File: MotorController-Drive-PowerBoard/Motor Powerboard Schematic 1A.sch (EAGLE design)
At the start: 72 parts, among them J3 APP_2POS_CONFIG5V_HORIZ, Q1 MOSFET-NCHANNELFQP30N06L, Q2 MOSFET-NCHANNELFQP30N06L, Q3 MOSFET-NCHANNELFQP30N06L, Q4 MOSFET-NCHANNELFQP30N06L, Q5 MOSFET-NCHANNELFQP30N06L, Q6 MOSFET-NCHANNELFQP30N06L, U1 NUP4201MR6

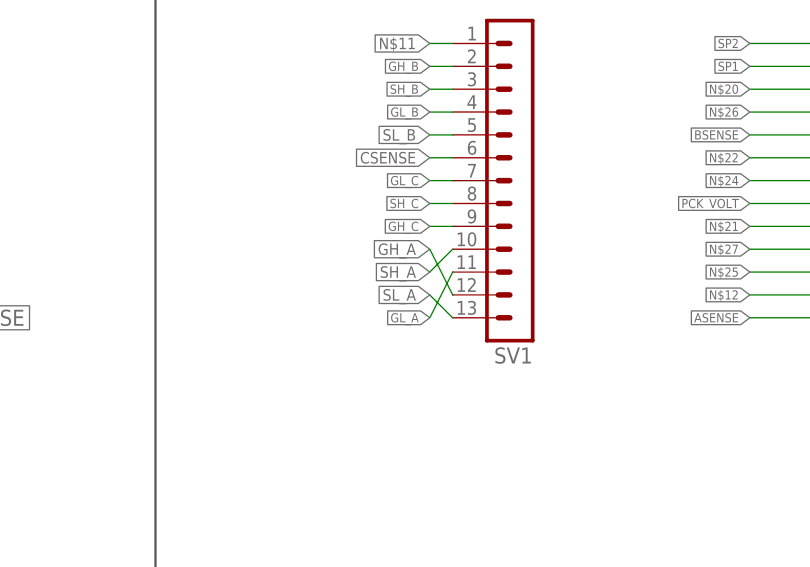
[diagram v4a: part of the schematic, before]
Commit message: Quick Routing and Labeling Fix
Straigtenned header names and made sure polygons stretched to same length on board.
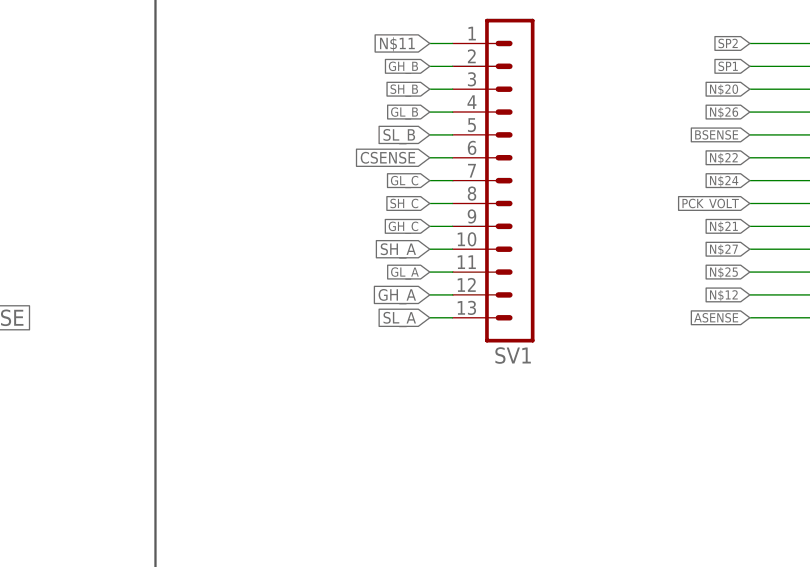
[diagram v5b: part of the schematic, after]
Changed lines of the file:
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@@
 <segment>
 <pinref part="SV1" gate="G$1" pin="13"/>
-<wire x1="172.72" y1="-43.18" x2="170.18" y2="-40.64" width="0.1524" layer="91"/>
-<label x="170.18" y="-40.64" size="1.27" layer="95" rot="R180" xref="yes"/>
+<wire x1="172.72" y1="-43.18" x2="170.18" y2="-43.18" width="0.1524" layer="91"/>
+<label x="170.18" y="-43.18" size="1.27" layer="95" rot="R180" xref="yes"/>
 </segment>
 </net>
@@
 <segment>
 <pinref part="SV1" gate="G$1" pin="11"/>
-<wire x1="172.72" y1="-38.1" x2="170.18" y2="-43.18" width="0.1524" layer="91"/>
-<label x="170.18" y="-43.18" size="1.016" layer="95" rot="R180" xref="yes"/>
+<wire x1="172.72" y1="-38.1" x2="170.18" y2="-38.1" width="0.1524" layer="91"/>
+<label x="170.18" y="-38.1" size="1.016" layer="95" rot="R180" xref="yes"/>
 </segment>
 </net>
@@
 <segment>
 <pinref part="SV1" gate="G$1" pin="12"/>
-<wire x1="172.72" y1="-40.64" x2="170.18" y2="-35.56" width="0.1524" layer="91"/>
-<label x="170.18" y="-35.56" size="1.27" layer="95" rot="R180" xref="yes"/>
+<wire x1="172.72" y1="-40.64" x2="170.18" y2="-40.64" width="0.1524" layer="91"/>
+<label x="170.18" y="-40.64" size="1.27" layer="95" rot="R180" xref="yes"/>
 </segment>
 </net>
@@
 <segment>
 <pinref part="SV1" gate="G$1" pin="10"/>
-<wire x1="172.72" y1="-35.56" x2="170.18" y2="-38.1" width="0.1524" layer="91"/>
-<label x="170.18" y="-38.1" size="1.27" layer="95" rot="R180" xref="yes"/>
+<wire x1="172.72" y1="-35.56" x2="170.18" y2="-35.56" width="0.1524" layer="91"/>
+<label x="170.18" y="-35.56" size="1.27" layer="95" rot="R180" xref="yes"/>
 </segment>
 </net>

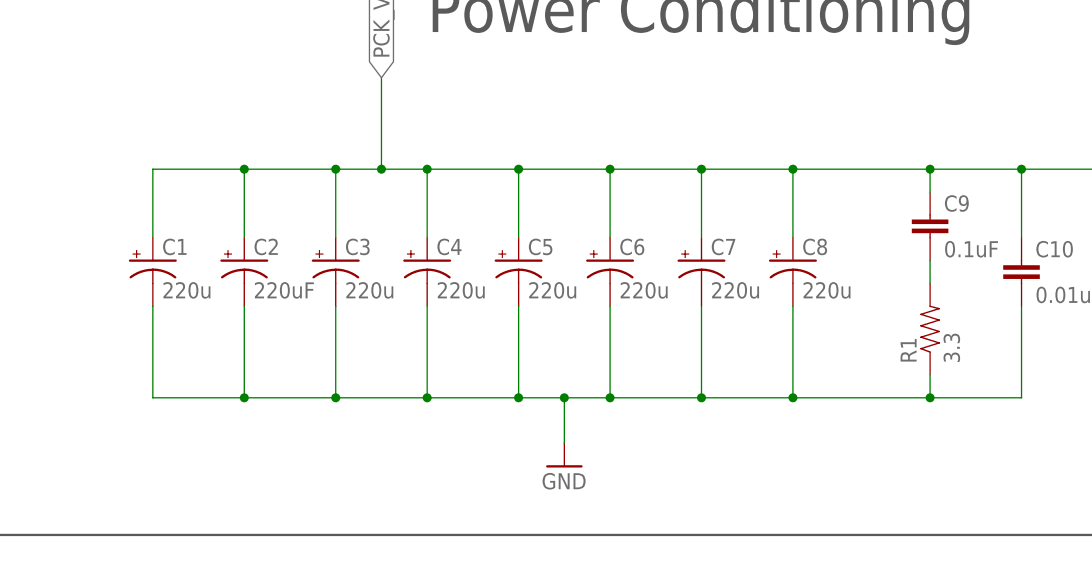
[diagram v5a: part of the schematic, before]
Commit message: Easier Viewing of Polygons. Replaced Caps
Caps now have a value of 470uF and all polygons are now easily visible so that all users can access information regarding polygons. Also all clearance issues have been resolved. Board still needs silk screen touches.
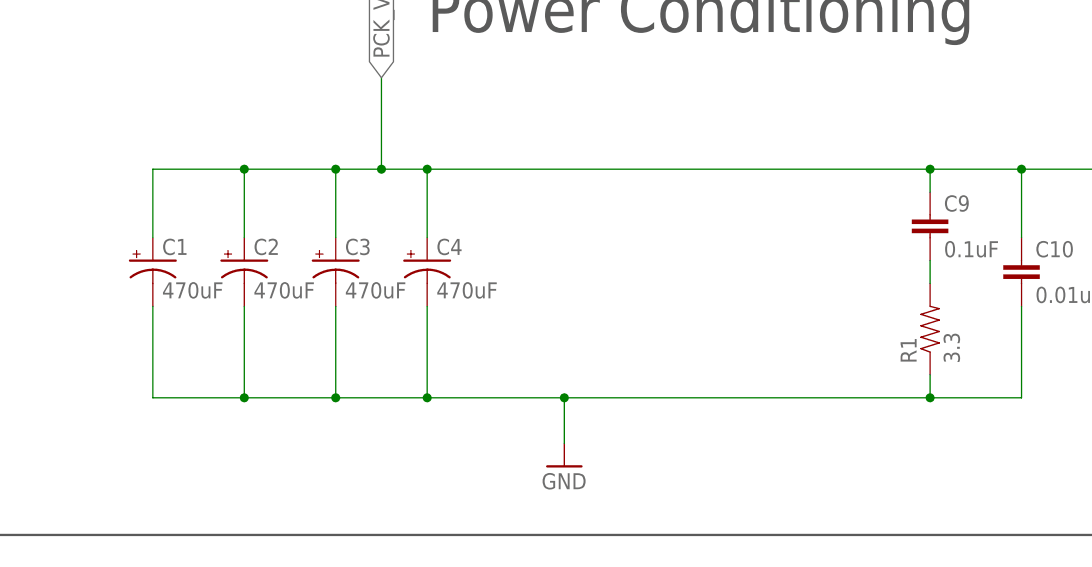
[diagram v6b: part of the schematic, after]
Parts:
- removed C5, C6, C7, C8: 220u, SparkFun-Passives:CAP_POLPTH4
- C1, C3, C4: value 220u -> 470uF
- C2: value 220uF -> 470uF
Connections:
- net GND: no longer C5.-, C6.-, C7.-, C8.-
- net PCK_VOLT: no longer C5.+, C6.+, C7.+, C8.+
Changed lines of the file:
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@@
 </classes>
 <parts>
-<part name="C1" library="SparkFun-Passives" deviceset="CAP_POL" device="PTH4" value="220u"/>
-<part name="C2" library="SparkFun-Passives" deviceset="CAP_POL" device="PTH4" value="220uF"/>
-<part name="C3" library="SparkFun-Passives" deviceset="CAP_POL" device="PTH4" value="220u"/>
-<part name="C4" library="SparkFun-Passives" deviceset="CAP_POL" device="PTH4" value="220u"/>
-<part name="C5" library="SparkFun-Passives" deviceset="CAP_POL" device="PTH4" value="220u"/>
-<part name="C6" library="SparkFun-Passives" deviceset="CAP_POL" device="PTH4" value="220u"/>
-<part name="C7" library="SparkFun-Passives" deviceset="CAP_POL" device="PTH4" value="220u"/>
-<part name="C8" library="SparkFun-Passives" deviceset="CAP_POL" device="PTH4" value="220u"/>
+<part name="C1" library="SparkFun-Passives" deviceset="CAP_POL" device="PTH4" value="470uF"/>
+<part name="C2" library="SparkFun-Passives" deviceset="CAP_POL" device="PTH4" value="470uF"/>
+<part name="C3" library="SparkFun-Passives" deviceset="CAP_POL" device="PTH4" value="470uF"/>
+<part name="C4" library="SparkFun-Passives" deviceset="CAP_POL" device="PTH4" value="470uF"/>
 <part name="R1" library="SparkFun-Passives" deviceset="RESISTOR" device="1206" value="3.3"/>
 <part name="GND1" library="SparkFun-Aesthetics" deviceset="GND" device=""/>
@@
 <instance part="C3" gate="G$1" x="-190.5" y="45.72"/>
 <instance part="C4" gate="G$1" x="-180.34" y="45.72"/>
-<instance part="C5" gate="G$1" x="-170.18" y="45.72"/>
-<instance part="C6" gate="G$1" x="-160.02" y="45.72"/>
-<instance part="C7" gate="G$1" x="-149.86" y="45.72"/>
-<instance part="C8" gate="G$1" x="-139.7" y="45.72"/>
 <instance part="R1" gate="G$1" x="-124.46" y="38.1" rot="R90"/>
 <instance part="GND1" gate="1" x="-165.1" y="22.86"/>
@@
 <wire x1="-210.82" y1="40.64" x2="-210.82" y2="30.48" width="0.1524" layer="91"/>
 <wire x1="-210.82" y1="30.48" x2="-200.66" y2="30.48" width="0.1524" layer="91"/>
-<pinref part="C8" gate="G$1" pin="-"/>
 <wire x1="-200.66" y1="30.48" x2="-190.5" y2="30.48" width="0.1524" layer="91"/>
 <wire x1="-190.5" y1="30.48" x2="-180.34" y2="30.48" width="0.1524" layer="91"/>
-<wire x1="-180.34" y1="30.48" x2="-170.18" y2="30.48" width="0.1524" layer="91"/>
-<wire x1="-170.18" y1="30.48" x2="-165.1" y2="30.48" width="0.1524" layer="91"/>
-<wire x1="-165.1" y1="30.48" x2="-160.02" y2="30.48" width="0.1524" layer="91"/>
-<wire x1="-160.02" y1="30.48" x2="-149.86" y2="30.48" width="0.1524" layer="91"/>
-<wire x1="-149.86" y1="30.48" x2="-139.7" y2="30.48" width="0.1524" layer="91"/>
-<wire x1="-139.7" y1="30.48" x2="-139.7" y2="40.64" width="0.1524" layer="91"/>
+<wire x1="-180.34" y1="30.48" x2="-165.1" y2="30.48" width="0.1524" layer="91"/>
 <pinref part="C3" gate="G$1" pin="-"/>
 <wire x1="-190.5" y1="40.64" x2="-190.5" y2="30.48" width="0.1524" layer="91"/>
@@
 <wire x1="-180.34" y1="40.64" x2="-180.34" y2="30.48" width="0.1524" layer="91"/>
 <junction x="-180.34" y="30.48"/>
-<pinref part="C5" gate="G$1" pin="-"/>
-<wire x1="-170.18" y1="40.64" x2="-170.18" y2="30.48" width="0.1524" layer="91"/>
-<junction x="-170.18" y="30.48"/>
-<pinref part="C6" gate="G$1" pin="-"/>
-<wire x1="-160.02" y1="40.64" x2="-160.02" y2="30.48" width="0.1524" layer="91"/>
-<junction x="-160.02" y="30.48"/>
-<pinref part="C7" gate="G$1" pin="-"/>
-<wire x1="-149.86" y1="40.64" x2="-149.86" y2="30.48" width="0.1524" layer="91"/>
-<junction x="-149.86" y="30.48"/>
 <pinref part="GND1" gate="1" pin="GND"/>
 <wire x1="-165.1" y1="25.4" x2="-165.1" y2="30.48" width="0.1524" layer="91"/>
@@
 <pinref part="R1" gate="G$1" pin="1"/>
 <wire x1="-124.46" y1="33.02" x2="-124.46" y2="30.48" width="0.1524" layer="91"/>
-<wire x1="-124.46" y1="30.48" x2="-139.7" y2="30.48" width="0.1524" layer="91"/>
-<junction x="-139.7" y="30.48"/>
+<wire x1="-124.46" y1="30.48" x2="-165.1" y2="30.48" width="0.1524" layer="91"/>
 <pinref part="C10" gate="G$1" pin="2"/>
 <wire x1="-114.3" y1="40.64" x2="-114.3" y2="30.48" width="0.1524" layer="91"/>
@@
 <net name="PCK_VOLT" class="0">
 <segment>
-<pinref part="C8" gate="G$1" pin="+"/>
-<wire x1="-139.7" y1="48.26" x2="-139.7" y2="55.88" width="0.1524" layer="91"/>
-<wire x1="-139.7" y1="55.88" x2="-149.86" y2="55.88" width="0.1524" layer="91"/>
 <pinref part="C1" gate="G$1" pin="+"/>
-<wire x1="-149.86" y1="55.88" x2="-160.02" y2="55.88" width="0.1524" layer="91"/>
-<wire x1="-160.02" y1="55.88" x2="-170.18" y2="55.88" width="0.1524" layer="91"/>
-<wire x1="-170.18" y1="55.88" x2="-180.34" y2="55.88" width="0.1524" layer="91"/>
 <wire x1="-180.34" y1="55.88" x2="-185.42" y2="55.88" width="0.1524" layer="91"/>
 <wire x1="-185.42" y1="55.88" x2="-190.5" y2="55.88" width="0.1524" layer="91"/>
@@
 <wire x1="-180.34" y1="48.26" x2="-180.34" y2="55.88" width="0.1524" layer="91"/>
 <junction x="-180.34" y="55.88"/>
-<pinref part="C5" gate="G$1" pin="+"/>
-<wire x1="-170.18" y1="48.26" x2="-170.18" y2="55.88" width="0.1524" layer="91"/>
-<junction x="-170.18" y="55.88"/>
-<pinref part="C6" gate="G$1" pin="+"/>
-<wire x1="-160.02" y1="48.26" x2="-160.02" y2="55.88" width="0.1524" layer="91"/>
-<junction x="-160.02" y="55.88"/>
-<pinref part="C7" gate="G$1" pin="+"/>
-<wire x1="-149.86" y1="48.26" x2="-149.86" y2="55.88" width="0.1524" layer="91"/>
-<junction x="-149.86" y="55.88"/>
 <wire x1="-185.42" y1="66.04" x2="-185.42" y2="55.88" width="0.1524" layer="91"/>
 <junction x="-185.42" y="55.88"/>
-<wire x1="-139.7" y1="55.88" x2="-124.46" y2="55.88" width="0.1524" layer="91"/>
-<junction x="-139.7" y="55.88"/>
+<wire x1="-180.34" y1="55.88" x2="-124.46" y2="55.88" width="0.1524" layer="91"/>
 <pinref part="C9" gate="G$1" pin="1"/>
 <wire x1="-124.46" y1="55.88" x2="-124.46" y2="53.34" width="0.1524" layer="91"/>

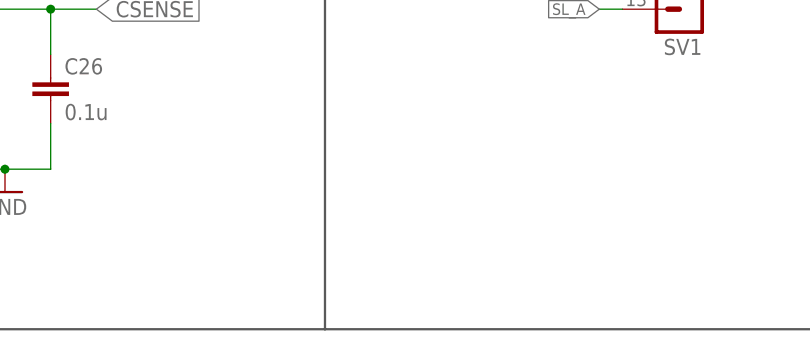
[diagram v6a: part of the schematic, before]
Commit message: Added Silkscreen and Bill of Materials
Bill of materials is now added and can be changed as time goes on. All objects on board have been smashed and names are fairly visible. Some areas around phase C are hard to read due to spacing. Silkscreen is mostly finished. Added Logo to schematic so that it could be placed on the board. Almost all testpoints are together for easy probing. They are all on the Left side of the board along the pin heads and 3 are seperated off from the group due to spacing issues.
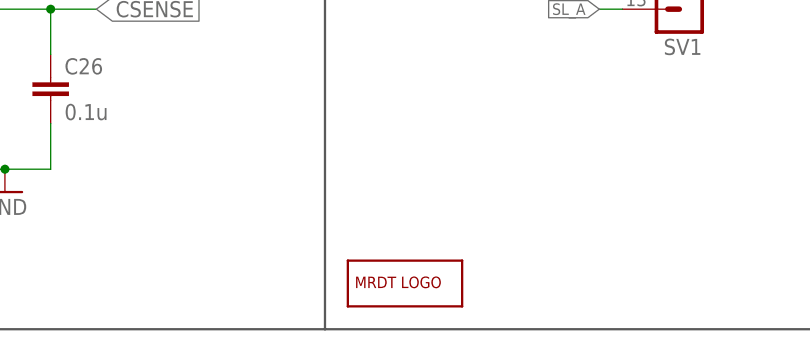
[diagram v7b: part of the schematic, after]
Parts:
- added LOGO1: MRDT_LOGO, MRDT-Hardware:MRDT_LOGO
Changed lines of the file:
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@@
 <part name="SV1" library="con-lstb" library_urn="urn:adsk.eagle:library:162" deviceset="MA13-1" device="" package3d_urn="urn:adsk.eagle:package:8367/1"/>
 <part name="SV2" library="con-lstb" library_urn="urn:adsk.eagle:library:162" deviceset="MA13-1" device="" package3d_urn="urn:adsk.eagle:package:8367/1"/>
+<part name="LOGO1" library="MRDT-Hardware" deviceset="MRDT_LOGO" device=""/>
 </parts>
 <sheets>
@@
 <instance part="SV1" gate="G$1" x="180.34" y="-27.94" rot="R180"/>
 <instance part="SV2" gate="G$1" x="223.52" y="-27.94" rot="R180"/>
+<instance part="LOGO1" gate="G$1" x="142.24" y="-76.2"/>
 </instances>
 <busses>
